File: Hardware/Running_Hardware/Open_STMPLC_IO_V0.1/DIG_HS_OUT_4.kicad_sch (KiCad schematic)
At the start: 24 parts, among them J15 Screw_Terminal_01x02, Q4 2N7002K, U18 TPS26600PWP, U19 NVTFS5124PLTAG

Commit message: Analog input section
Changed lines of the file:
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@@
 			(effects
 				(font
-					(size 1.27 1.27)
+					(size 1 1)
 				)
 				(justify left)
@@
 			(effects
 				(font
-					(size 1.27 1.27)
+					(size 1 1)
 				)
 				(justify left)
@@
 			(effects
 				(font
-					(size 1.27 1.27)
+					(size 1 1)
 				)
 				(justify left)
@@
 			(effects
 				(font
-					(size 1.27 1.27)
+					(size 1 1)
 				)
 				(justify left)

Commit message: GSM Module add
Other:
- title: (none) -> Open_PLC_IO
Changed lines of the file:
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@@
 	(generator_version "9.0")
 	(paper "A4")
+	(title_block
+		(title "Open_PLC_IO")
+		(date "2026-04-01")
+		(rev "0.1")
+	)
 	(rectangle
 		(start 13.97 13.97)

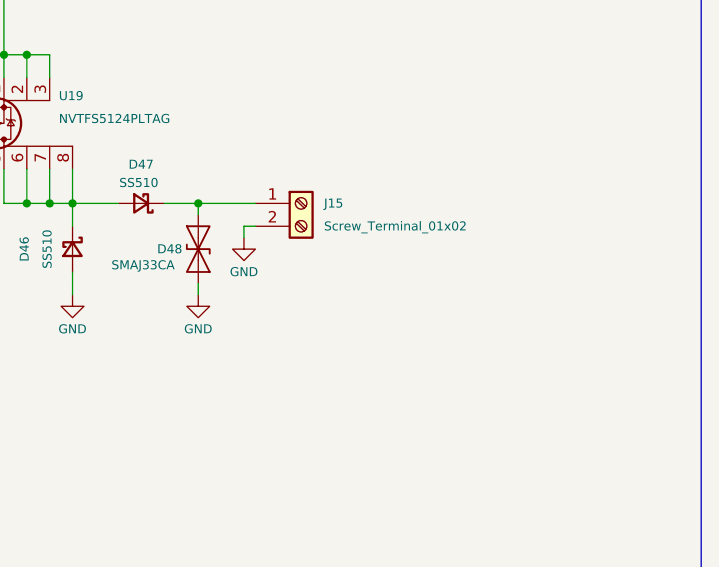
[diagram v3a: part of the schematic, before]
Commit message: Main PCB schematic changes V0.1
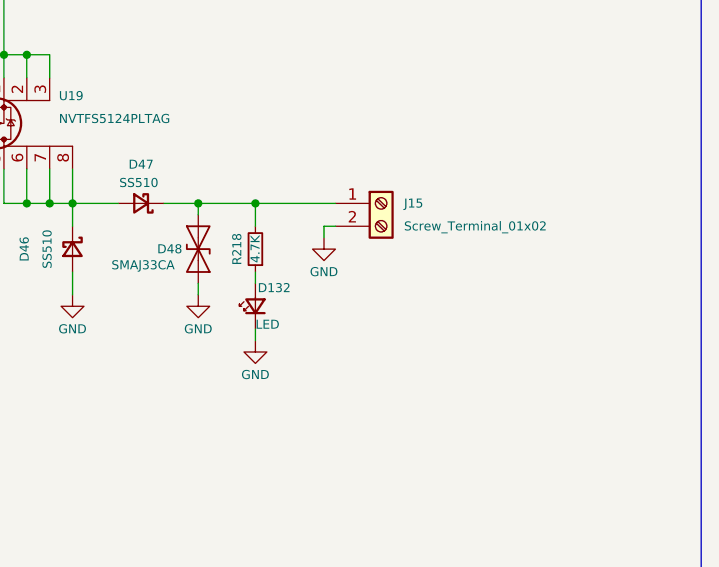
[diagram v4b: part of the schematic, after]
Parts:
- added D132: LED, LED_SMD:LED_0603_1608Metric_Pad1.05x0.95mm_HandSolder, symbol Device:LED_Small
- added R218: 4.7K, Resistor_SMD:R_0603_1608Metric_Pad0.98x0.95mm_HandSolder, symbol Device:R_Small
- C31, C32, C34: footprint (none) -> Capacitor_SMD:C_0603_1608Metric_Pad1.08x0.95mm_HandSolder
- C33: footprint (none) -> Capacitor_SMD:C_0805_2012Metric_Pad1.18x1.45mm_HandSolder
- D45: footprint (none) -> Diode_SMD:D_SOD-123
- J15: footprint (none) -> TerminalBlock_Phoenix:TerminalBlock_Phoenix_MKDS-1,5-2_1x02_P5.00mm_Horizontal
- R109, R110, R111, R112: footprint (none) -> Resistor_SMD:R_0603_1608Metric_Pad0.98x0.95mm_HandSolder
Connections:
- net GND: now also D132.1 (K)
- net at D47.1 (K), D48.1 (A1), J15.1 (Pin_1): now also R218.2
- new net: D132.2 (A), R218.1
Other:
- title: Open_PLC_IO -> Open_STMPLC_IO
- moved on the sheet: J15

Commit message: New DXF update
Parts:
- J15: footprint TerminalBlock_Phoenix:TerminalBlock_Phoenix_MKDS-1,5-2_1x02_P5.00mm_Horizontal -> TerminalBlock_Phoenix:TerminalBlock_Phoenix_MKDS-1-2-3.81_1x02_P3.81mm_Horizontal
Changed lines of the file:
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@@
 			)
 		)
-		(property "Footprint" "TerminalBlock_Phoenix:TerminalBlock_Phoenix_MKDS-1,5-2_1x02_P5.00mm_Horizontal"
+		(property "Footprint" "TerminalBlock_Phoenix:TerminalBlock_Phoenix_MKDS-1-2-3.81_1x02_P3.81mm_Horizontal"
 			(at 246.38 88.9 0)
 			(effects

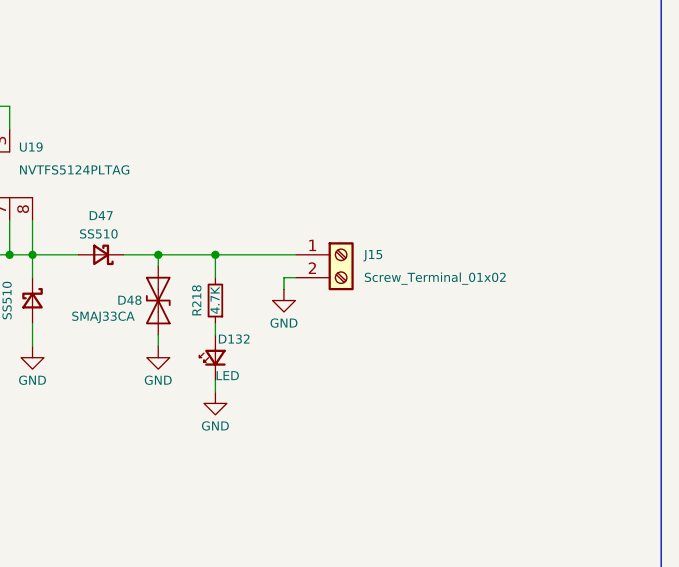
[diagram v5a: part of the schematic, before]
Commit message: Common GND terminal changes
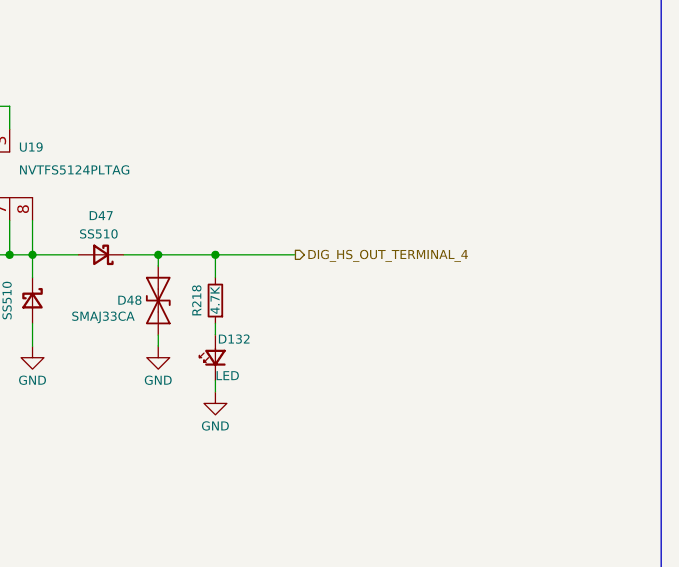
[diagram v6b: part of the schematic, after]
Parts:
- removed J15: Screw_Terminal_01x02, TerminalBlock_Phoenix:TerminalBlock_Phoenix_MKDS-1-2-3.81_1x02_P3.81mm_Horizontal, symbol Connector:Screw_Terminal_01x02
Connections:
- net DIG_HS_OUT_TERMINAL_4: now reaches D47.1 (K), D48.1 (A1), R218.2
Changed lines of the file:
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@@
-	(wire
-		(pts
-			(xy 240.03 92.71) (xy 240.03 91.44)
-		)
-		(stroke
-			(width 0)
-			(type default)
-		)
-	)
 	(wire
 		(pts
@@
 		(pts
 			(xy 212.09 88.9) (xy 209.55 88.9)
-		)
-		(stroke
-			(width 0)
-			(type default)
-		)
-	)
-	(wire
-		(pts
-			(xy 240.03 91.44) (xy 241.3 91.44)
 		)
 		(stroke
@@
 		(shape output)
 		(at 123.19 80.01 0)
+		(effects
+			(font
+				(size 1 1)
+			)
+			(justify left)
+		)
+	)
+	(hierarchical_label "DIG_HS_OUT_TERMINAL_4"
+		(shape output)
+		(at 241.3 88.9 0)
 		(effects
 			(font
@@
 				(path "/4d6787b6-1f4f-4098-b70b-d936e584350b/893b5029-7450-4d12-87c5-e23e52a6c6a4"
 					(reference "#PWR0103")
-					(unit 1)
-				)
-			)
-		)
-	)
-	(symbol
-		(lib_id "Connector:Screw_Terminal_01x02")
-		(at 246.38 88.9 0)
-		(unit 1)
-		(exclude_from_sim no)
-		(in_bom yes)
-		(on_board yes)
-		(dnp no)
-		(fields_autoplaced yes)
-		(property "Reference" "J15"
-			(at 248.92 88.8999 0)
-			(effects
-				(font
-					(size 1 1)
-				)
-				(justify left)
-			)
-		)
-		(property "Value" "Screw_Terminal_01x02"
-			(at 248.92 91.4399 0)
-			(effects
-				(font
-					(size 1 1)
-				)
-				(justify left)
-			)
-		)
-		(property "Footprint" "TerminalBlock_Phoenix:TerminalBlock_Phoenix_MKDS-1-2-3.81_1x02_P3.81mm_Horizontal"
-			(at 246.38 88.9 0)
-			(effects
-				(font
-					(size 1.27 1.27)
-				)
-				(hide yes)
-			)
-		)
-		(property "Datasheet" "~"
-			(at 246.38 88.9 0)
-			(effects
-				(font
-					(size 1.27 1.27)
-				)
-				(hide yes)
-			)
-		)
-		(property "Description" "Generic screw terminal, single row, 01x02, script generated (kicad-library-utils/schlib/autogen/connector/)"
-			(at 246.38 88.9 0)
-			(effects
-				(font
-					(size 1.27 1.27)
-				)
-				(hide yes)
-			)
-		)
-		(pin "1"
-		)
-		(pin "2"
-		)
-		(instances
-			(project "Open_STMPLC_IO_V0.1"
-				(path "/4d6787b6-1f4f-4098-b70b-d936e584350b/893b5029-7450-4d12-87c5-e23e52a6c6a4"
-					(reference "J15")
 					(unit 1)
 				)
@@
 					(unit 1)
 				)
-			)
-		)
-	)
-	(symbol
-		(lib_id "power:GND")
-		(at 240.03 92.71 0)
-		(unit 1)
-		(exclude_from_sim no)
-		(in_bom yes)
-		(on_board yes)
-		(dnp no)
-		(property "Reference" "#PWR0108"
-			(at 240.03 99.06 0)
-			(effects
-				(font
-					(size 1 1)
-				)
-				(hide yes)
-			)
-		)
-		(property "Value" "GND"
-			(at 240.03 96.52 0)
-			(effects
-				(font
-					(size 1 1)
-				)
-			)
-		)
-		(property "Footprint" ""
-			(at 240.03 92.71 0)
-			(effects
-				(font
-					(size 1.27 1.27)
-				)
-				(hide yes)
-			)
-		)
-		(property "Datasheet" ""
-			(at 240.03 92.71 0)
-			(effects
-				(font
-					(size 1.27 1.27)
-				)
-				(hide yes)
-			)
-		)
-		(property "Description" "Power symbol creates a global label with name \"GND\" , ground"
-			(at 240.03 92.71 0)
-			(effects
-				(font
-					(size 1.27 1.27)
-				)
-				(hide yes)
-			)
-		)
-		(pin "1"
-		)
-		(instances
-			(project "Open_STMPLC_IO_V0.1"
-				(path "/4d6787b6-1f4f-4098-b70b-d936e584350b/893b5029-7450-4d12-87c5-e23e52a6c6a4"
-					(reference "#PWR0108")
-					(unit 1)
-				)

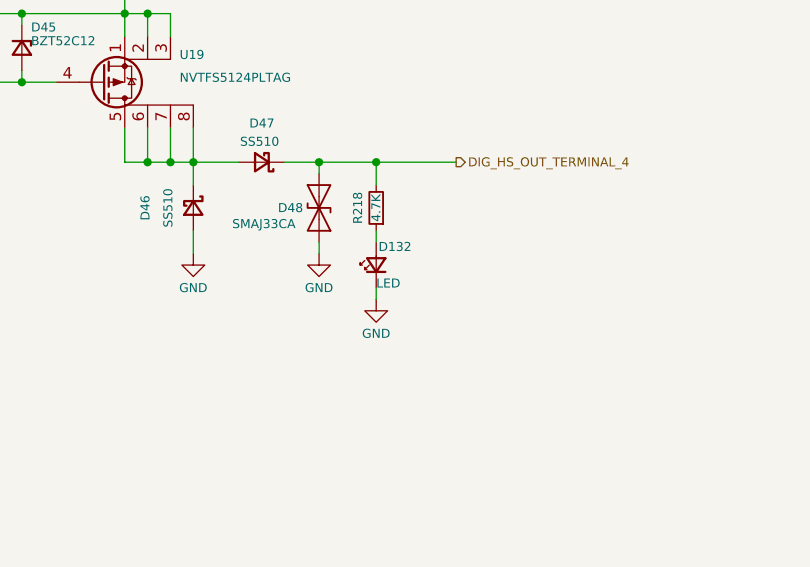
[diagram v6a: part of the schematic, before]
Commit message: Schematic updates
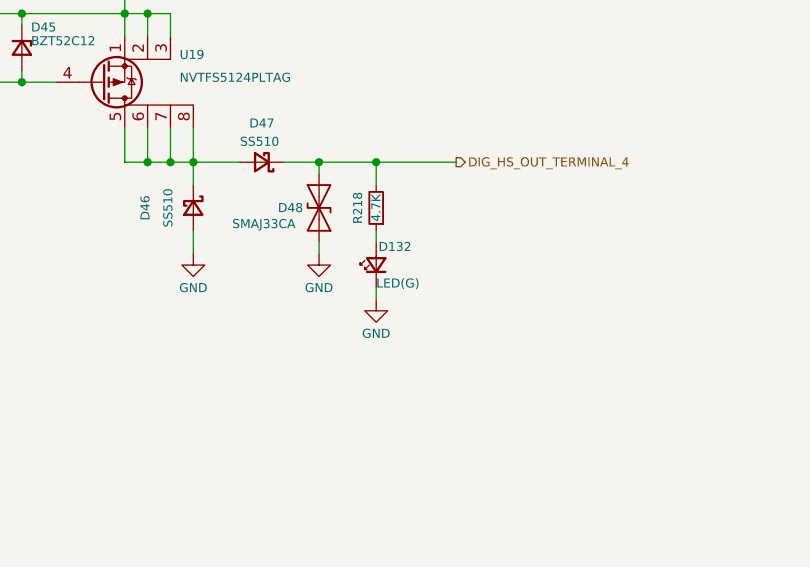
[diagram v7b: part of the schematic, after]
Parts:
- D132: value LED -> LED(G)
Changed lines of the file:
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@@
 			)
 		)
-		(property "Value" "LED"
+		(property "Value" "LED(G)"
 			(at 232.41 102.362 90)
 			(effects
